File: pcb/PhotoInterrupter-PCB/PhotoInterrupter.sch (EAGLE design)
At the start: 7 parts

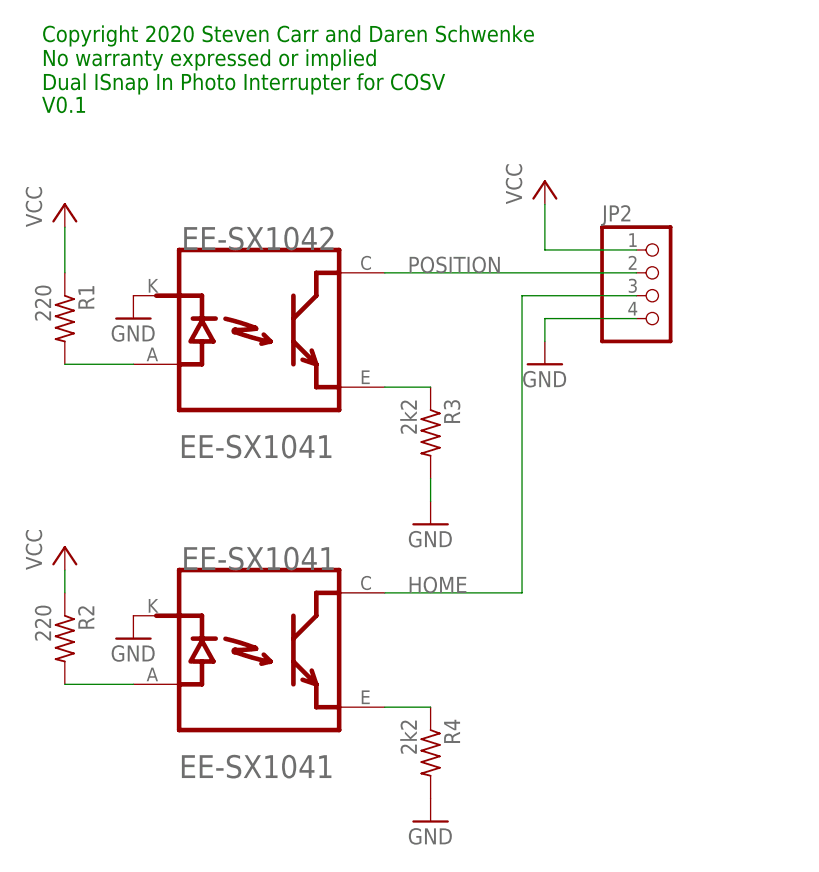
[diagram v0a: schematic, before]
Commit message: Snap In Photo Interrupter Enhancements.
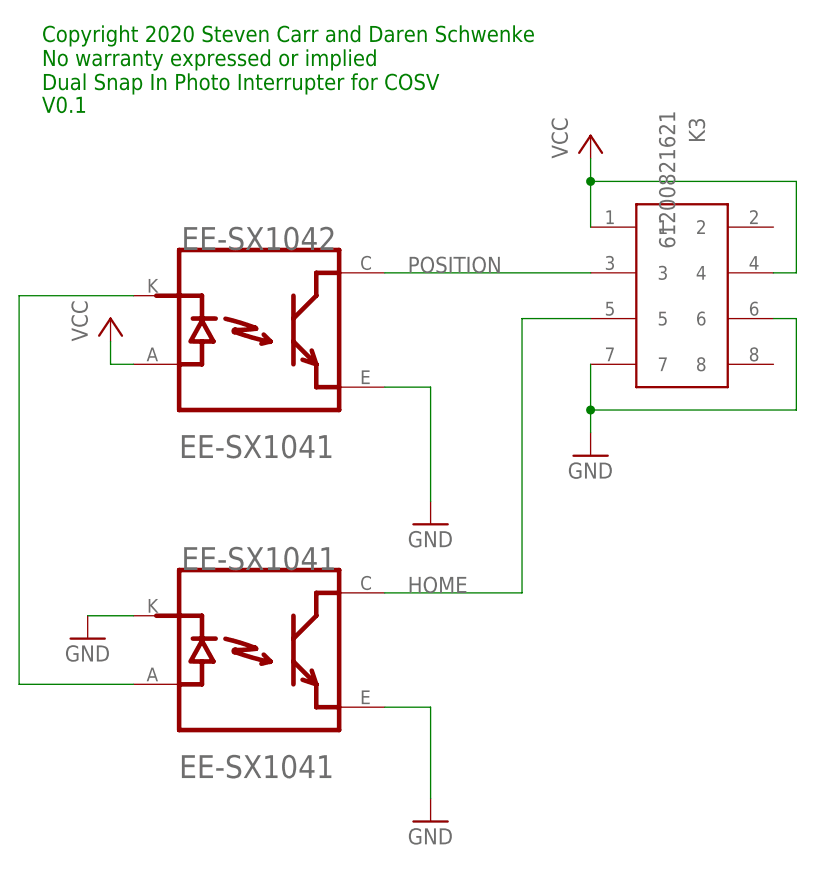
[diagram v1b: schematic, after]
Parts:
- removed JP2: (no value), pinhead:PINHD-1X4
- removed R1, R2: 220, resistor:R-US_R1206
- removed R3, R4: 2k2, resistor:R-US_R1206
- added K3: 61200821621, Wuerth_Elektronik_eiCan_05_Box_Header_IDC_Connectors_1_2:61200821621
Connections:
- removed net N$11: EE-SX1041.E, R4.1
- removed net N$2: EE-SX1041.A, R2.2
- removed net N$3: EE-SX1042.E, R3.1
- net GND: now also EE-SX1041.E, EE-SX1042.E, K3.6, K3.7; no longer EE-SX1042.K, JP2.4, R3.2, R4.2
- net HOME: now also K3.5; no longer JP2.3
- net N$1: now also EE-SX1041.A, EE-SX1042.K; no longer EE-SX1042.A, R1.2
- net POSITION: now also K3.3; no longer JP2.2
- net VCC: now also EE-SX1042.A, K3.1, K3.4; no longer JP2.1, R1.1, R2.1
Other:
- note added: "Copyright 2020 Steven Carr and Daren Schwenke No warranty expressed or implied Dual Snap In Photo Interrupter for COSV"
- note removed: "Copyright 2020 Steven Carr and Daren Schwenke No warranty expressed or implied Dual ISnap In Photo Interrupter for COSV"
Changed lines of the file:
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@@
 </classes>
 <parts>
-<part name="R1" library="resistor" deviceset="R-US_" device="R1206" value="220"/>
-<part name="R2" library="resistor" deviceset="R-US_" device="R1206" value="220"/>
-<part name="P+1" library="supply1" deviceset="VCC" device=""/>
 <part name="P+2" library="supply1" deviceset="VCC" device=""/>
 <part name="GND1" library="supply1" deviceset="GND" device=""/>
 <part name="GND2" library="supply1" deviceset="GND" device=""/>
-<part name="R3" library="resistor" deviceset="R-US_" device="R1206" value="2k2"/>
-<part name="R4" library="resistor" deviceset="R-US_" device="R1206" value="2k2"/>
-<part name="GND3" library="supply1" deviceset="GND" device=""/>
-<part name="GND4" library="supply1" deviceset="GND" device=""/>
-<part name="JP2" library="pinhead" deviceset="PINHD-1X4" device=""/>
 <part name="P+5" library="supply1" deviceset="VCC" device=""/>
 <part name="GND5" library="supply1" deviceset="GND" device=""/>
 <part name="EE-SX1042" library="PhotoInterrupter" deviceset="OMRON_ELECTRONICS_INC-EMC_DIV_EE-SX1041" device="OMRON_ELECTRONICS_INC-EMC_DIV_EE-SX1041_0_0"/>
 <part name="EE-SX1041" library="PhotoInterrupter" deviceset="OMRON_ELECTRONICS_INC-EMC_DIV_EE-SX1041" device="OMRON_ELECTRONICS_INC-EMC_DIV_EE-SX1041_0_0"/>
+<part name="GND3" library="supply1" deviceset="GND" device=""/>
+<part name="K3" library="Wuerth_Elektronik_eiCan_05_Box_Header_IDC_Connectors_1_2" deviceset="61200821621" device=""/>
 </parts>
 <sheets>
@@
 <text x="25.4" y="91.44" size="1.778" layer="91">Copyright 2020 Steven Carr and Daren Schwenke
 No warranty expressed or implied
-Dual ISnap In Photo Interrupter for COSV</text>
+Dual Snap In Photo Interrupter for COSV</text>
 <text x="25.4" y="88.9" size="1.778" layer="91">V0.1</text>
 </plain>
 <instances>
-<instance part="R1" gate="G$1" x="27.94" y="66.04" rot="R270"/>
-<instance part="R2" gate="G$1" x="27.94" y="30.48" rot="R270"/>
-<instance part="P+1" gate="VCC" x="27.94" y="78.74"/>
-<instance part="P+2" gate="VCC" x="27.94" y="40.64"/>
+<instance part="P+2" gate="VCC" x="33.02" y="66.04"/>
 <instance part="GND1" gate="1" x="68.58" y="43.18"/>
 <instance part="GND2" gate="1" x="68.58" y="10.16"/>
-<instance part="R3" gate="G$1" x="68.58" y="53.34" rot="R270"/>
-<instance part="R4" gate="G$1" x="68.58" y="17.78" rot="R270"/>
-<instance part="GND3" gate="1" x="35.56" y="66.04"/>
-<instance part="GND4" gate="1" x="35.56" y="30.48"/>
-<instance part="JP2" gate="A" x="93.98" y="68.58"/>
-<instance part="P+5" gate="VCC" x="81.28" y="81.28"/>
-<instance part="GND5" gate="1" x="81.28" y="60.96"/>
+<instance part="P+5" gate="VCC" x="86.36" y="86.36"/>
+<instance part="GND5" gate="1" x="86.36" y="50.8"/>
 <instance part="EE-SX1042" gate="G$0" x="38.1" y="76.2"/>
 <instance part="EE-SX1041" gate="G$0" x="38.1" y="40.64"/>
+<instance part="GND3" gate="1" x="30.48" y="30.48"/>
+<instance part="K3" gate="G$1" x="96.52" y="71.12" rot="R270"/>
 </instances>
 <busses>
@@
 <net name="VCC" class="0">
 <segment>
-<pinref part="R1" gate="G$1" pin="1"/>
-<pinref part="P+1" gate="VCC" pin="VCC"/>
-<wire x1="27.94" y1="76.2" x2="27.94" y2="71.12" width="0.1524" layer="91"/>
+<pinref part="P+5" gate="VCC" pin="VCC"/>
+<wire x1="86.36" y1="83.82" x2="86.36" y2="81.28" width="0.1524" layer="91"/>
+<pinref part="K3" gate="G$1" pin="1"/>
+<pinref part="K3" gate="G$1" pin="4"/>
+<wire x1="86.36" y1="81.28" x2="86.36" y2="76.2" width="0.1524" layer="91"/>
+<wire x1="106.68" y1="71.12" x2="109.22" y2="71.12" width="0.1524" layer="91"/>
+<wire x1="109.22" y1="71.12" x2="109.22" y2="81.28" width="0.1524" layer="91"/>
+<wire x1="109.22" y1="81.28" x2="86.36" y2="81.28" width="0.1524" layer="91"/>
+<junction x="86.36" y="81.28"/>
 </segment>
 <segment>
-<pinref part="R2" gate="G$1" pin="1"/>
+<pinref part="EE-SX1042" gate="G$0" pin="A"/>
 <pinref part="P+2" gate="VCC" pin="VCC"/>
-<wire x1="27.94" y1="35.56" x2="27.94" y2="38.1" width="0.1524" layer="91"/>
-</segment>
-<segment>
-<pinref part="P+5" gate="VCC" pin="VCC"/>
-<wire x1="81.28" y1="78.74" x2="81.28" y2="73.66" width="0.1524" layer="91"/>
-<pinref part="JP2" gate="A" pin="1"/>
-<wire x1="81.28" y1="73.66" x2="91.44" y2="73.66" width="0.1524" layer="91"/>
+<wire x1="35.56" y1="60.96" x2="33.02" y2="60.96" width="0.1524" layer="91"/>
+<wire x1="33.02" y1="60.96" x2="33.02" y2="63.5" width="0.1524" layer="91"/>
 </segment>
 </net>
@@
 <segment>
 <pinref part="GND5" gate="1" pin="GND"/>
-<wire x1="81.28" y1="63.5" x2="81.28" y2="66.04" width="0.1524" layer="91"/>
-<pinref part="JP2" gate="A" pin="4"/>
-<wire x1="91.44" y1="66.04" x2="81.28" y2="66.04" width="0.1524" layer="91"/>
+<wire x1="86.36" y1="53.34" x2="86.36" y2="55.88" width="0.1524" layer="91"/>
+<pinref part="K3" gate="G$1" pin="7"/>
+<pinref part="K3" gate="G$1" pin="6"/>
+<wire x1="86.36" y1="55.88" x2="86.36" y2="60.96" width="0.1524" layer="91"/>
+<wire x1="106.68" y1="66.04" x2="109.22" y2="66.04" width="0.1524" layer="91"/>
+<wire x1="109.22" y1="66.04" x2="109.22" y2="55.88" width="0.1524" layer="91"/>
+<wire x1="109.22" y1="55.88" x2="86.36" y2="55.88" width="0.1524" layer="91"/>
+<junction x="86.36" y="55.88"/>
 </segment>
 <segment>
 <pinref part="GND1" gate="1" pin="GND"/>
-<pinref part="R3" gate="G$1" pin="2"/>
-<wire x1="68.58" y1="45.72" x2="68.58" y2="48.26" width="0.1524" layer="91"/>
-</segment>
-<segment>
-<pinref part="GND2" gate="1" pin="GND"/>
-<pinref part="R4" gate="G$1" pin="2"/>
+<wire x1="68.58" y1="58.42" x2="63.5" y2="58.42" width="0.1524" layer="91"/>
+<pinref part="EE-SX1042" gate="G$0" pin="E"/>
+<wire x1="68.58" y1="58.42" x2="68.58" y2="45.72" width="0.1524" layer="91"/>
 </segment>
 <segment>
 <pinref part="GND3" gate="1" pin="GND"/>
-<pinref part="EE-SX1042" gate="G$0" pin="K"/>
+<pinref part="EE-SX1041" gate="G$0" pin="K"/>
+<wire x1="30.48" y1="33.02" x2="35.56" y2="33.02" width="0.1524" layer="91"/>
 </segment>
 <segment>
-<pinref part="GND4" gate="1" pin="GND"/>
-<pinref part="EE-SX1041" gate="G$0" pin="K"/>
+<wire x1="68.58" y1="22.86" x2="63.5" y2="22.86" width="0.1524" layer="91"/>
+<pinref part="EE-SX1041" gate="G$0" pin="E"/>
+<pinref part="GND2" gate="1" pin="GND"/>
+<wire x1="68.58" y1="12.7" x2="68.58" y2="22.86" width="0.1524" layer="91"/>
 </segment>
 </net>
@@
 <segment>
 <label x="66.04" y="35.56" size="1.778" layer="95"/>
-<wire x1="78.74" y1="35.56" x2="78.74" y2="68.58" width="0.1524" layer="91"/>
-<pinref part="JP2" gate="A" pin="3"/>
-<wire x1="78.74" y1="68.58" x2="91.44" y2="68.58" width="0.1524" layer="91"/>
+<wire x1="78.74" y1="35.56" x2="78.74" y2="66.04" width="0.1524" layer="91"/>
+<wire x1="78.74" y1="66.04" x2="86.36" y2="66.04" width="0.1524" layer="91"/>
 <wire x1="63.5" y1="35.56" x2="78.74" y2="35.56" width="0.1524" layer="91"/>
 <pinref part="EE-SX1041" gate="G$0" pin="C"/>
+<pinref part="K3" gate="G$1" pin="5"/>
 </segment>
 </net>
 <net name="POSITION" class="0">
 <segment>
-<wire x1="63.5" y1="71.12" x2="91.44" y2="71.12" width="0.1524" layer="91"/>
+<wire x1="63.5" y1="71.12" x2="86.36" y2="71.12" width="0.1524" layer="91"/>
 <label x="66.04" y="71.12" size="1.778" layer="95"/>
-<pinref part="JP2" gate="A" pin="2"/>
 <pinref part="EE-SX1042" gate="G$0" pin="C"/>
-</segment>
-</net>
-<net name="N$3" class="0">
-<segment>
-<pinref part="R3" gate="G$1" pin="1"/>
-<wire x1="68.58" y1="58.42" x2="63.5" y2="58.42" width="0.1524" layer="91"/>
-<pinref part="EE-SX1042" gate="G$0" pin="E"/>
-</segment>
-</net>
-<net name="N$11" class="0">
-<segment>
-<pinref part="R4" gate="G$1" pin="1"/>
-<wire x1="68.58" y1="22.86" x2="63.5" y2="22.86" width="0.1524" layer="91"/>
-<pinref part="EE-SX1041" gate="G$0" pin="E"/>
+<pinref part="K3" gate="G$1" pin="3"/>
 </segment>
 </net>
 <net name="N$1" class="0">
 <segment>
-<pinref part="R1" gate="G$1" pin="2"/>
-<wire x1="35.56" y1="60.96" x2="27.94" y2="60.96" width="0.1524" layer="91"/>
-<pinref part="EE-SX1042" gate="G$0" pin="A"/>
+<pinref part="EE-SX1042" gate="G$0" pin="K"/>
+<wire x1="35.56" y1="68.58" x2="22.86" y2="68.58" width="0.1524" layer="91"/>
+<wire x1="22.86" y1="68.58" x2="22.86" y2="25.4" width="0.1524" layer="91"/>
+<pinref part="EE-SX1041" gate="G$0" pin="A"/>
+<wire x1="22.86" y1="25.4" x2="35.56" y2="25.4" width="0.1524" layer="91"/>
 </segment>
 </net>
-<net name="N$2" class="0">
-<segment>
-<pinref part="R2" gate="G$1" pin="2"/>
-<wire x1="35.56" y1="25.4" x2="27.94" y2="25.4" width="0.1524" layer="91"/>
-<pinref part="EE-SX1041" gate="G$0" pin="A"/>
-</segment>
-</net>

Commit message: Label parts properly HY870-L and EE-SX1042 components
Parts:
- renumbered EE-SX1041 to HY870-L
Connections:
- net GND: now also K3.8
- net VCC: now also K3.2
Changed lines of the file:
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@@
 <part name="GND5" library="supply1" deviceset="GND" device=""/>
 <part name="EE-SX1042" library="PhotoInterrupter" deviceset="OMRON_ELECTRONICS_INC-EMC_DIV_EE-SX1041" device="OMRON_ELECTRONICS_INC-EMC_DIV_EE-SX1041_0_0"/>
-<part name="EE-SX1041" library="PhotoInterrupter" deviceset="OMRON_ELECTRONICS_INC-EMC_DIV_EE-SX1041" device="OMRON_ELECTRONICS_INC-EMC_DIV_EE-SX1041_0_0"/>
+<part name="HY870-L" library="PhotoInterrupter" deviceset="OMRON_ELECTRONICS_INC-EMC_DIV_EE-SX1041" device="OMRON_ELECTRONICS_INC-EMC_DIV_EE-SX1041_0_0"/>
 <part name="GND3" library="supply1" deviceset="GND" device=""/>
 <part name="K3" library="Wuerth_Elektronik_eiCan_05_Box_Header_IDC_Connectors_1_2" deviceset="61200821621" device=""/>
@@
 <instance part="GND5" gate="1" x="86.36" y="50.8"/>
 <instance part="EE-SX1042" gate="G$0" x="38.1" y="76.2"/>
-<instance part="EE-SX1041" gate="G$0" x="38.1" y="40.64"/>
+<instance part="HY870-L" gate="G$0" x="38.1" y="40.64"/>
 <instance part="GND3" gate="1" x="30.48" y="30.48"/>
 <instance part="K3" gate="G$1" x="96.52" y="71.12" rot="R270"/>
@@
 <wire x1="86.36" y1="81.28" x2="86.36" y2="76.2" width="0.1524" layer="91"/>
 <wire x1="106.68" y1="71.12" x2="109.22" y2="71.12" width="0.1524" layer="91"/>
-<wire x1="109.22" y1="71.12" x2="109.22" y2="81.28" width="0.1524" layer="91"/>
+<wire x1="109.22" y1="71.12" x2="109.22" y2="76.2" width="0.1524" layer="91"/>
+<wire x1="109.22" y1="76.2" x2="109.22" y2="81.28" width="0.1524" layer="91"/>
 <wire x1="109.22" y1="81.28" x2="86.36" y2="81.28" width="0.1524" layer="91"/>
 <junction x="86.36" y="81.28"/>
+<pinref part="K3" gate="G$1" pin="2"/>
+<wire x1="106.68" y1="76.2" x2="109.22" y2="76.2" width="0.1524" layer="91"/>
+<junction x="109.22" y="76.2"/>
 </segment>
 <segment>
@@
 <wire x1="86.36" y1="55.88" x2="86.36" y2="60.96" width="0.1524" layer="91"/>
 <wire x1="106.68" y1="66.04" x2="109.22" y2="66.04" width="0.1524" layer="91"/>
-<wire x1="109.22" y1="66.04" x2="109.22" y2="55.88" width="0.1524" layer="91"/>
+<wire x1="109.22" y1="66.04" x2="109.22" y2="60.96" width="0.1524" layer="91"/>
+<wire x1="109.22" y1="60.96" x2="109.22" y2="55.88" width="0.1524" layer="91"/>
 <wire x1="109.22" y1="55.88" x2="86.36" y2="55.88" width="0.1524" layer="91"/>
 <junction x="86.36" y="55.88"/>
+<pinref part="K3" gate="G$1" pin="8"/>
+<wire x1="106.68" y1="60.96" x2="109.22" y2="60.96" width="0.1524" layer="91"/>
+<junction x="109.22" y="60.96"/>
 </segment>
 <segment>
@@
 <segment>
 <pinref part="GND3" gate="1" pin="GND"/>
-<pinref part="EE-SX1041" gate="G$0" pin="K"/>
+<pinref part="HY870-L" gate="G$0" pin="K"/>
 <wire x1="30.48" y1="33.02" x2="35.56" y2="33.02" width="0.1524" layer="91"/>
 </segment>
 <segment>
 <wire x1="68.58" y1="22.86" x2="63.5" y2="22.86" width="0.1524" layer="91"/>
-<pinref part="EE-SX1041" gate="G$0" pin="E"/>
+<pinref part="HY870-L" gate="G$0" pin="E"/>
 <pinref part="GND2" gate="1" pin="GND"/>
 <wire x1="68.58" y1="12.7" x2="68.58" y2="22.86" width="0.1524" layer="91"/>
@@
 <wire x1="78.74" y1="66.04" x2="86.36" y2="66.04" width="0.1524" layer="91"/>
 <wire x1="63.5" y1="35.56" x2="78.74" y2="35.56" width="0.1524" layer="91"/>
-<pinref part="EE-SX1041" gate="G$0" pin="C"/>
+<pinref part="HY870-L" gate="G$0" pin="C"/>
 <pinref part="K3" gate="G$1" pin="5"/>
 </segment>
@@
 <wire x1="35.56" y1="68.58" x2="22.86" y2="68.58" width="0.1524" layer="91"/>
 <wire x1="22.86" y1="68.58" x2="22.86" y2="25.4" width="0.1524" layer="91"/>
-<pinref part="EE-SX1041" gate="G$0" pin="A"/>
+<pinref part="HY870-L" gate="G$0" pin="A"/>
 <wire x1="22.86" y1="25.4" x2="35.56" y2="25.4" width="0.1524" layer="91"/>
 </segment>
